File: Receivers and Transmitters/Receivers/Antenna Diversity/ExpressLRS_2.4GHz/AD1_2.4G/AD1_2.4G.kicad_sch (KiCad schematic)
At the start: 8 parts, among them J1 Conn_01x04_Socket, J3 Conn_01x04_Pin, U1 TPS7A4701xRGW

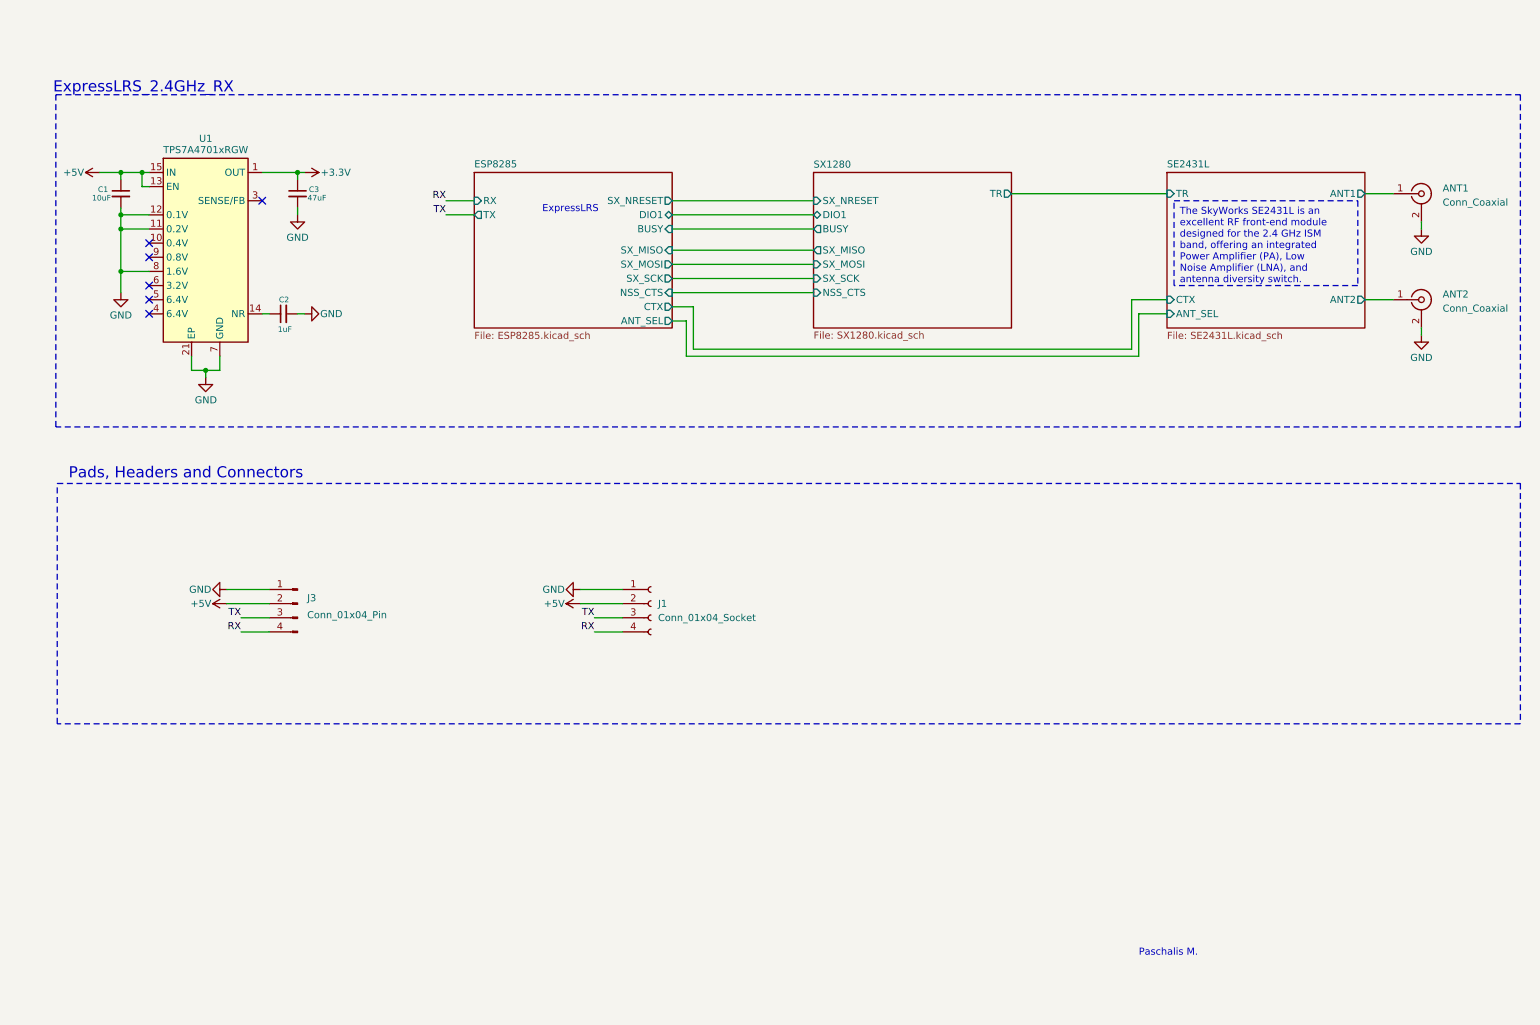
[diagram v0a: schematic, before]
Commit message: Update Antenna Diversity (AD1_2.4G), True Antenna Diversity (TD1_2.4G), and Gemini Mode transmitter (G_TX1): Modify KiCad files, add BOMs and production files; update images, docs, videos, and README; remove outdated Mechanical CAD file
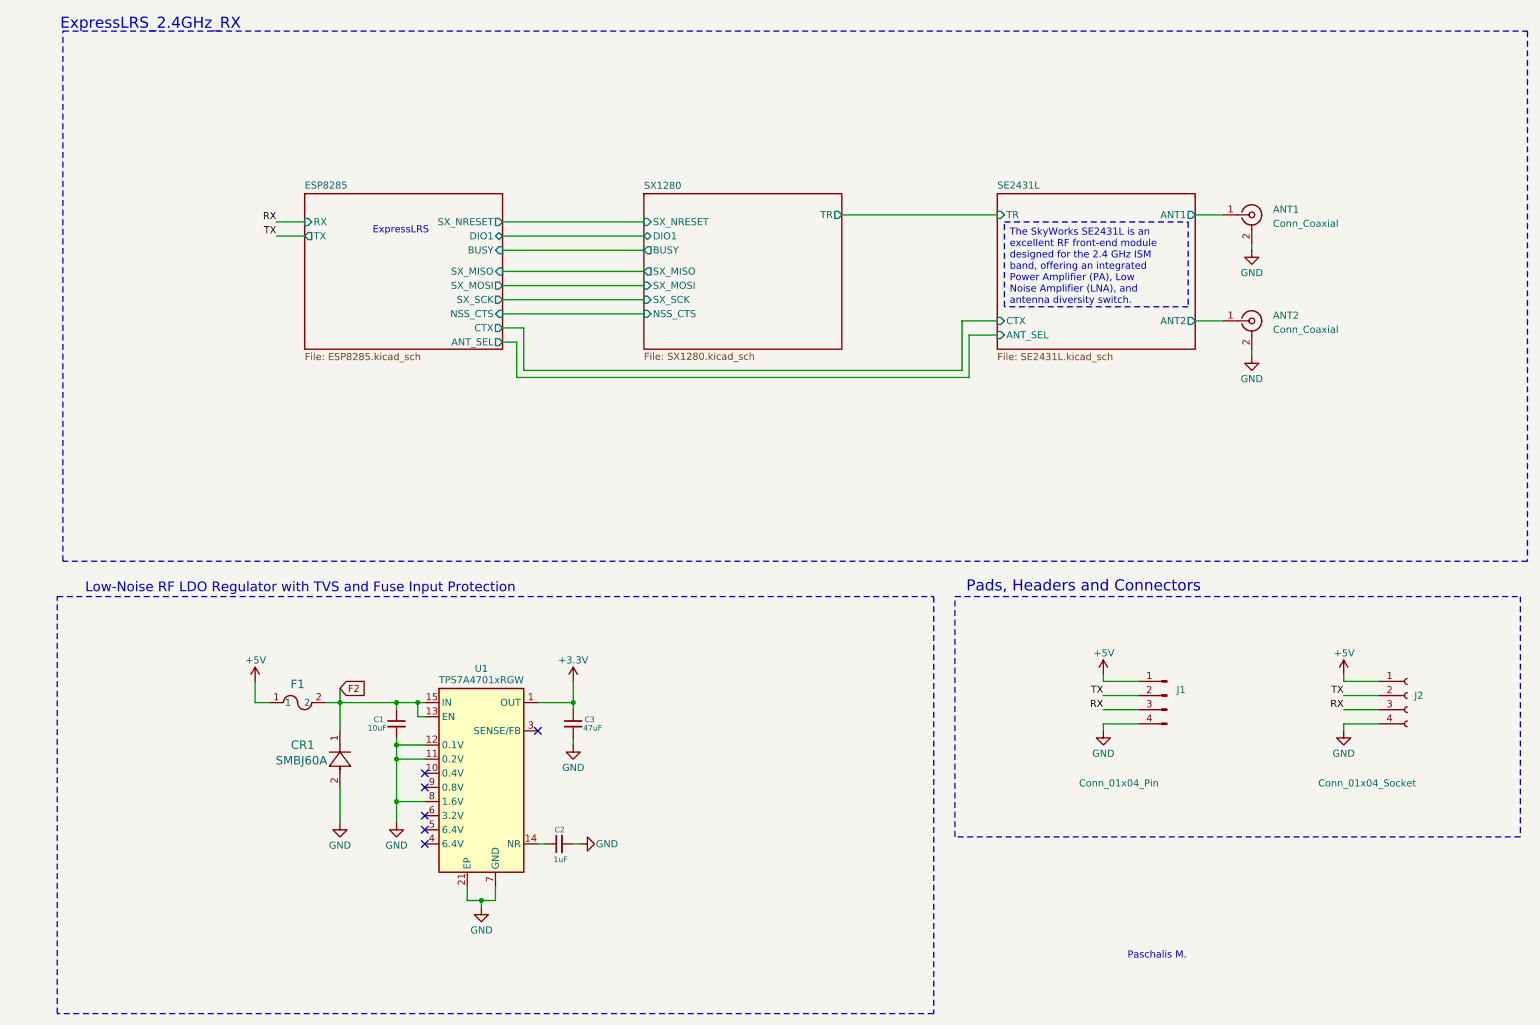
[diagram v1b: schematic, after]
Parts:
- removed J1: Conn_01x04_Socket, Connector_Harwin:Harwin_M20-89004xx_1x04_P2.54mm_Horizontal, symbol Connector:Conn_01x04_Socket
- removed J3: Conn_01x04_Pin, Connector_JST:JST_GH_SM04B-GHS-TB_1x04-1MP_P1.25mm_Horizontal, symbol Connector:Conn_01x04_Pin
- added CR1: SMBJ60A, ul_SMBJ60A:SMBJSeries_LTF, symbol ul_SMBJ60A:SMBJ60A
- added F1: MF-PSMF020X-2, ul_MF-PSMF020X-2:FUSE_F020X_BRN, symbol ul_MF-PSMF020X-2:MF-PSMF020X-2
- added J1: Conn_01x04_Pin, Connector_JST:JST_GH_SM04B-GHS-TB_1x04-1MP_P1.25mm_Horizontal, symbol Connector:Conn_01x04_Pin
- added J2: Conn_01x04_Socket, Connector_Harwin:Harwin_M20-89004xx_1x04_P2.54mm_Horizontal, symbol Connector:Conn_01x04_Socket
- C1, C2, C3: footprint Capacitor_SMD:C_0805_2012Metric_Pad1.18x1.45mm_HandSolder -> Capacitor_SMD:C_0603_1608Metric_Pad1.08x0.95mm_HandSolder
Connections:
- net +5V: now also F1.1, J1.1 (Pin_1), J2.1 (Pin_1); no longer C1.1, U1.13 (EN), U1.15 (IN), U1.16 (IN)
- net GND: now also CR1.2, J1.4 (Pin_4), J2.4 (Pin_4)
- net RX: now also J1.3 (Pin_3), J2.3 (Pin_3)
- net TX: now also J1.2 (Pin_2), J2.2 (Pin_2)
- new net F2: C1.1, CR1.1, F1.2, U1.13 (EN), U1.15 (IN), U1.16 (IN)
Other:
- note added: "Low-Noise RF LDO Regulator with TVS and Fuse Input Protection"
- company: https://github.com/Paschalis | TeodoraMiu -> https://github.com/Paschalis
- moved on the sheet: ANT1, ANT2
